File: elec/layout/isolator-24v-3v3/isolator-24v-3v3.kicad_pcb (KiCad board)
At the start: 2 copper layers, 11 parts, among them U12 2.2µF ±10% 25V X7R, U2 8.2kΩ ±1% 62.5mW, U3 10kΩ ±1% 62.5mW, U5 10µH ±20%, U6 10µF ±10% 25V X5R, U7 10µF ±10% 25V X5R, U9 2.2µF ±10% 25V X7R

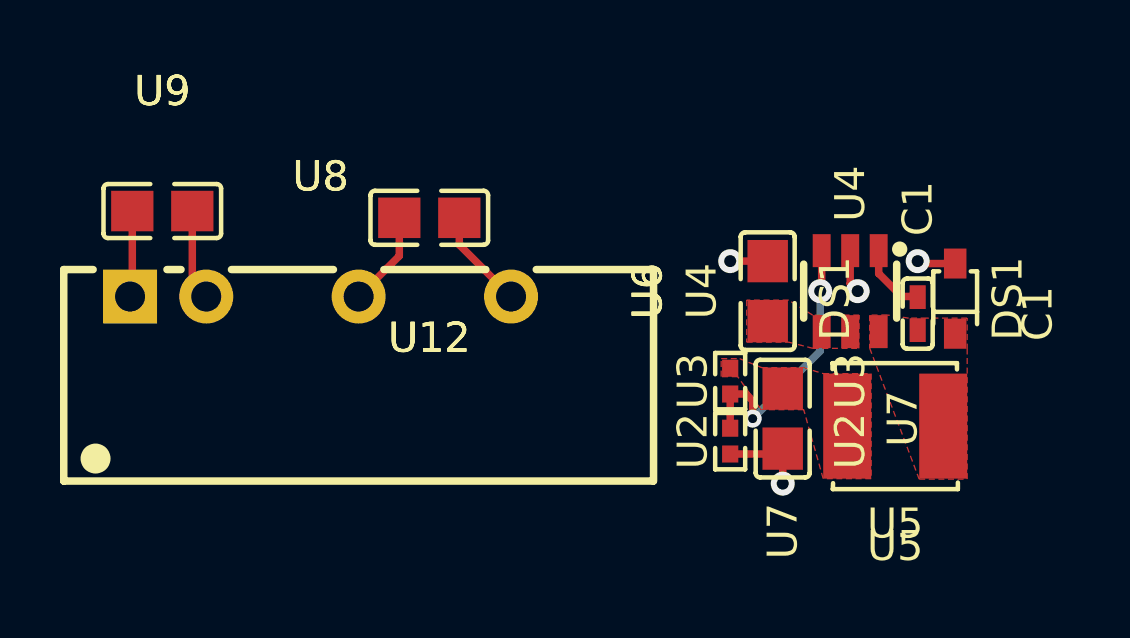
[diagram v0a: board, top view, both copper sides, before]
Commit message: update layouts to kicad 9
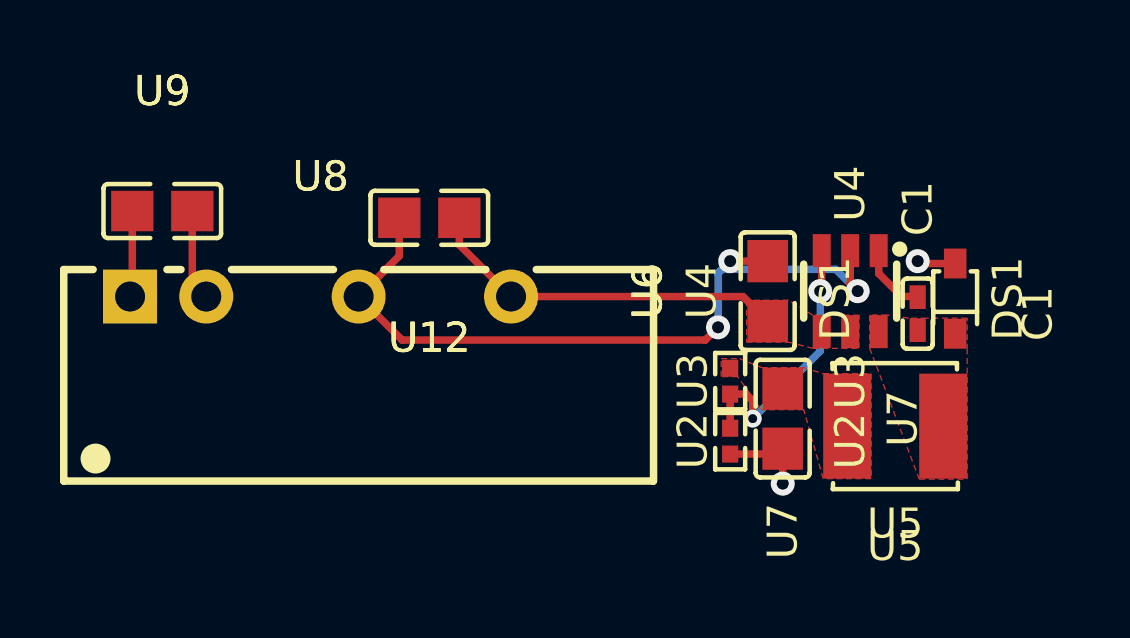
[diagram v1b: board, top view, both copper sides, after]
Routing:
- net gnd-1: track 5.89 -> 26.0 mm, vias 2 -> 3
- net hv: track 3.34 -> 12.2 mm

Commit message: update LED gpio pin
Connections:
- net cathode renamed SW
- U12 pad 2: gnd-1 -> gnd-2
- U3 pad 1: hv-2 -> hv-1
- U4 pad 2: gnd-1 -> gnd-2
- U5 pad 2: hv-2 -> hv-1
- U6 pad 2: gnd-1 -> gnd-2
- U7 pad 1: hv-2 -> hv-1
- U8 pad 1: hv-1 -> hv-2
- U8 pad 2: gnd-2 -> gnd-1
- U8 pad 4: gnd-1 -> gnd-2
- U9 pad 1: hv-1 -> hv-2
- U9 pad 2: gnd-2 -> gnd-1
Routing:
- net gnd-2: track 3.04 -> 26.0 mm, vias 0 -> 3
- net gnd-1: track 26.0 -> 3.04 mm, vias 3 -> 0
- net hv-2: track 0.00 -> 2.88 mm
- net hv-1: track 2.88 -> 0.00 mm

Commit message: restore layout files
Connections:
- net SW renamed cathode
- U12 pad 2: gnd-2 -> gnd-1
- U3 pad 1: hv-1 -> hv-2
- U4 pad 2: gnd-2 -> gnd-1
- U5 pad 2: hv-1 -> hv-2
- U6 pad 2: gnd-2 -> gnd-1
- U7 pad 1: hv-1 -> hv-2
- U8 pad 1: hv-2 -> hv-1
- U8 pad 2: gnd-1 -> gnd-2
- U8 pad 4: gnd-2 -> gnd-1
- U9 pad 1: hv-2 -> hv-1
- U9 pad 2: gnd-1 -> gnd-2
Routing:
- net gnd-2: track 26.0 -> 3.04 mm, vias 3 -> 0
- net gnd-1: track 3.04 -> 26.0 mm, vias 0 -> 3
- net hv-2: track 2.88 -> 0.00 mm
- net hv-1: track 0.00 -> 2.88 mm

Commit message: building frozen
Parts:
- added D1: , atopile:LED0603-RD-c81ffb, F.Cu at (94.2, 87.3)
- added R1: 1kΩ ±1% 62.5mW, atopile:R0402-56259e, F.Cu at (97.5, 87.2)
- U12: value 2.2µF ±10% 25V X7R -> 10µF ±10% 25V X5R
- U2: value 8.2kΩ ±1% 62.5mW -> 10kΩ ±1% 62.5mW
- U6: value 10µF ±10% 25V X5R -> 4.7µF ±10% 25V X5R
- U8: footprint atopile:PWRM-TH_BXXXXS-2WR3-d8b2fb -> atopile:PWRM-TH_BXXXXS-2WR2-87119e
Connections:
- net cathode renamed SW
- net line renamed FB
- DS1 pad 2: gnd -> gnd-2
- U12 pad 2: gnd-1 -> gnd
- U2 pad 2: gnd -> gnd-2
- U3 pad 1: hv-2 -> hv-1
- U4 pad 2: gnd-1 -> gnd
- U5 pad 2: hv-2 -> hv-1
- U6 pad 2: gnd-1 -> gnd
- U7 pad 1: hv-2 -> hv-1
- U7 pad 2: gnd -> gnd-2
- U8 pad 1: hv-1 -> hv-2
- U8 pad 2: gnd-2 -> gnd-1
- U8 pad 4: gnd-1 -> gnd
- U9 pad 1: hv-1 -> hv-2
- U9 pad 2: gnd-2 -> gnd-1
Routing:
- net gnd: track 4.28 -> 28.9 mm, vias 2 -> 3
- net gnd-1: track 26.0 -> 3.04 mm, vias 3 -> 0
- net hv-2: track 0.00 -> 2.88 mm
- net hv-1: track 2.88 -> 0.00 mm
- net hv: track 12.2 -> 14.5 mm
- net cathode: track 0.00 -> 2.11 mm
- net gnd-2: track 3.04 -> 4.28 mm, vias 0 -> 2

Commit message: building locally to fix frozen builds
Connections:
- net SW renamed buck_converter-cathode
- net cathode renamed isolated_supply.led-cathode
- D1 pad 2: hv -> hv-2
- DS1 pad 2: gnd-2 -> gnd-1
- U12 pad 1: hv -> hv-2
- U2 pad 2: gnd-2 -> gnd-1
- U3 pad 1: hv-1 -> hv
- U4 pad 4: hv -> hv-2
- U4 pad 5: hv -> hv-2
- U5 pad 2: hv-1 -> hv
- U6 pad 1: hv -> hv-2
- U7 pad 1: hv-1 -> hv
- U7 pad 2: gnd-2 -> gnd-1
- U8 pad 1: hv-2 -> hv-1
- U8 pad 2: gnd-1 -> gnd-2
- U8 pad 6: hv -> hv-2
- U9 pad 1: hv-2 -> hv-1
- U9 pad 2: gnd-1 -> gnd-2
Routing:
- net hv: track 14.5 -> 0.00 mm
- net hv-2: track 2.88 -> 14.5 mm
- net hv-1: track 0.00 -> 2.88 mm
- net gnd-2: track 4.28 -> 3.04 mm, vias 2 -> 0
- net gnd-1: track 3.04 -> 4.28 mm, vias 0 -> 2
- added copper zone on F.Cu, net hv
- removed copper zone on F.Cu, net hv-2
